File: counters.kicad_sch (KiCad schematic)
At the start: 22 parts, among them J10 Conn_01x10_Socket, J11 Conn_01x06_Socket, J12 Conn_01x10_Socket, J13 Conn_01x03_Socket, J8 Conn_01x10_Socket, J9 Conn_01x06_Socket, SW1 SW_Push, SW2 SW_Push, U3 SSR, U8 bin-to-dec, U9 bin-to-dec

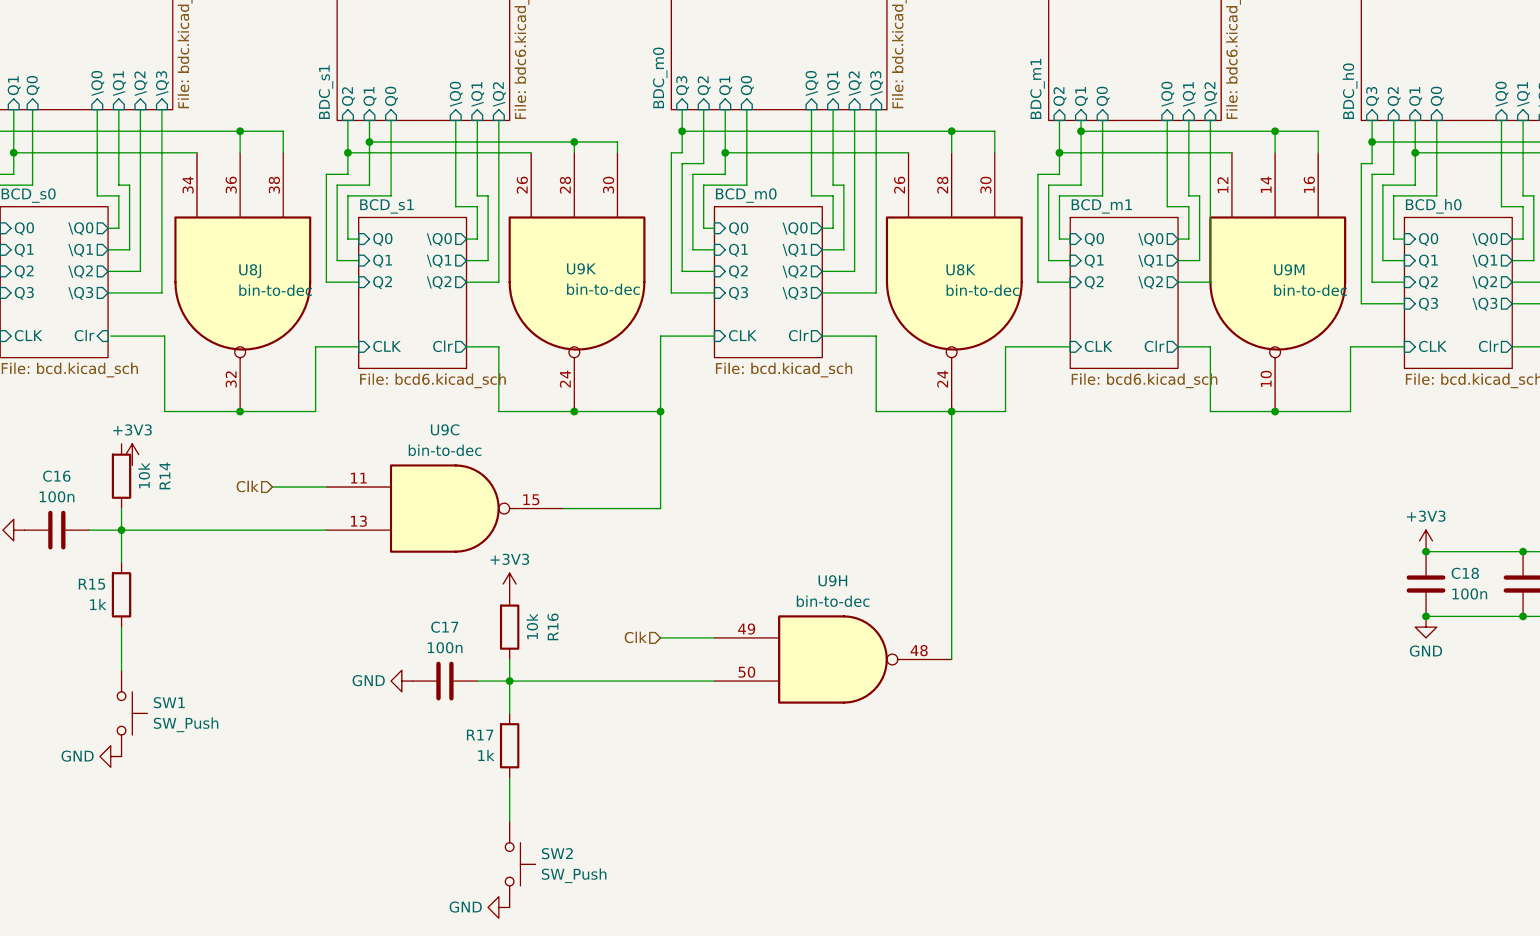
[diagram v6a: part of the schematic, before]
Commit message: some routing on main board
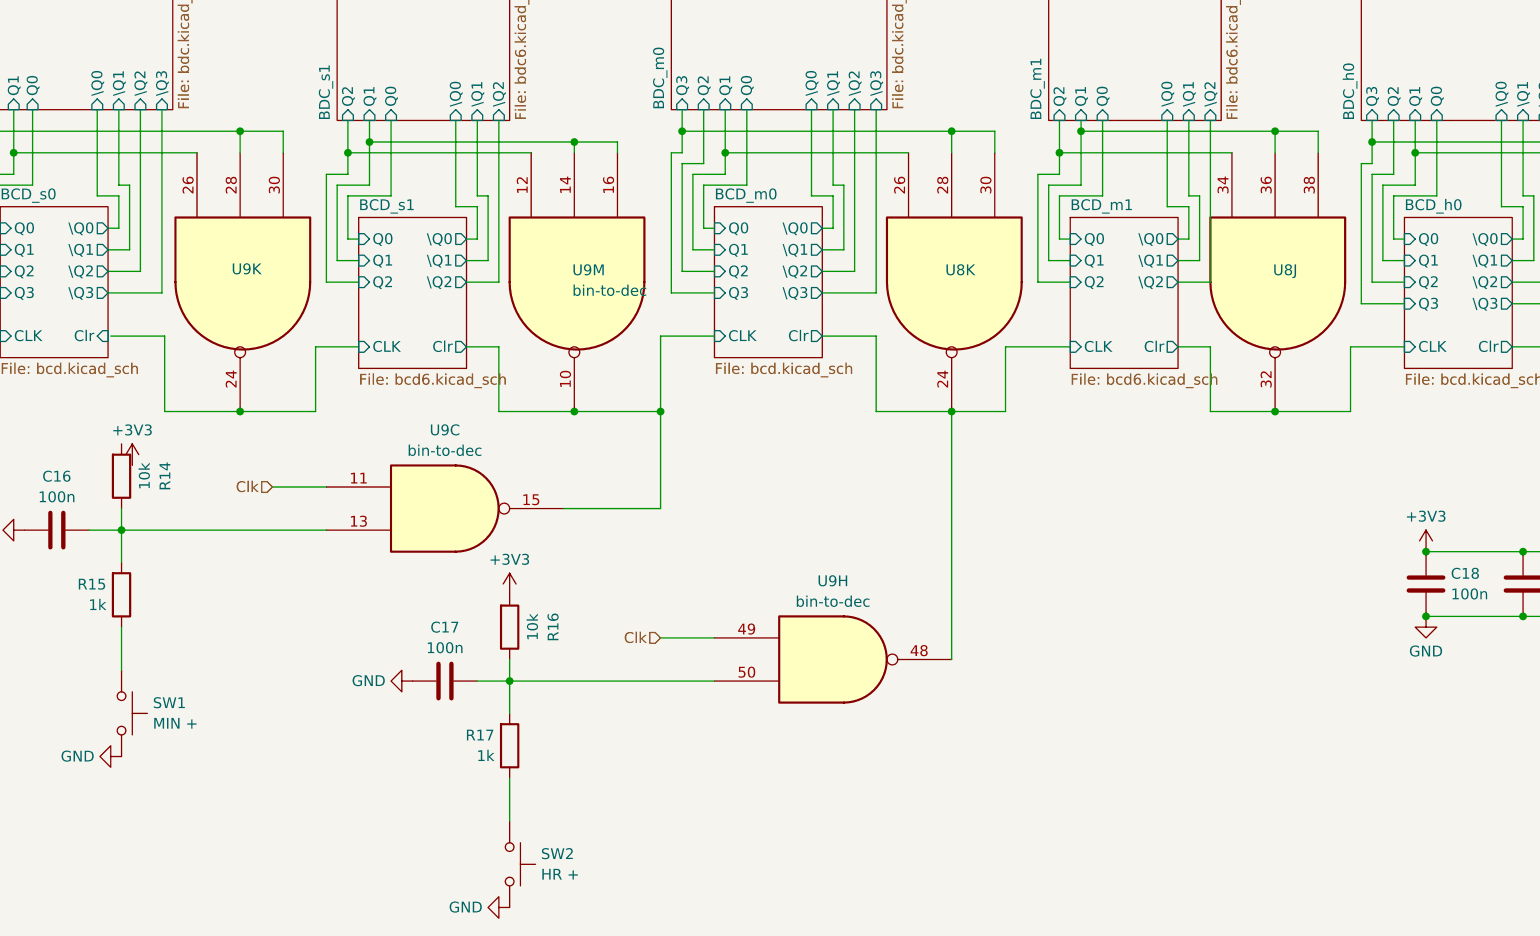
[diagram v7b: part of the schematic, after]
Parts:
- R14, R15, R16, R17: footprint Resistor_SMD:R_0402_1005Metric -> Resistor_SMD:R_0603_1608Metric
- SW1: value SW_Push -> MIN +; footprint Button_Switch_SMD:SW_Push_1P1T_NO_CK_PTS125Sx43PSMTR -> Button_Switch_SMD:SW_SPST_EVQPE1; LCSC Part # (none) -> C720477
- SW2: value SW_Push -> HR +; footprint Button_Switch_SMD:SW_Push_1P1T_NO_CK_PTS125Sx43PSMTR -> Button_Switch_SMD:SW_SPST_EVQPE1; LCSC Part # (none) -> C720477
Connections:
- net BCD_h0/CLK: now also U8.32; no longer U9.10
- net BCD_m0/CLK: now also U9.10; no longer U9.24
- net BCD_m1/Q1: now also U8.36, U8.38; no longer U9.14, U9.16
- net BCD_m1/Q2: now also U8.34; no longer U9.12
- net BCD_s0/Q1: now also U9.26; no longer U8.34
- net BCD_s0/Q3: now also U9.28, U9.30; no longer U8.36, U8.38
- net BCD_s1/CLK: now also U9.24; no longer U8.32
- net BCD_s1/Q1: now also U9.14, U9.16; no longer U9.28, U9.30
- net BCD_s1/Q2: now also U9.12; no longer U9.26
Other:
- moved on the sheet: U8J, U9K, U9M
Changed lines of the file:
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@@
 	(paper "A4")
 	(junction
+		(at 52.07 130.81)
+		(diameter 0)
+		(color 0 0 0 0)
+	)
+	(junction
 		(at 91.44 99.06)
 		(diameter 0)
@@
 	)
 	(junction
-		(at 104.14 97.79)
-		(diameter 0)
-		(color 0 0 0 0)
-	)
-	(junction
-		(at 91.44 130.81)
+		(at 173.99 130.81)
 		(diameter 0)
 		(color 0 0 0 0)
 	)
 	(junction
-		(at 173.99 130.81)
+		(at 104.14 97.79)
 		(diameter 0)
 		(color 0 0 0 0)
@@
 	)
 	(junction
+		(at 91.44 130.81)
+		(diameter 0)
+		(color 0 0 0 0)
+	)
+	(junction
 		(at 148.59 100.33)
 		(diameter 0)
@@
 	)
 	(junction
-		(at 52.07 130.81)
-		(diameter 0)
-		(color 0 0 0 0)
-	)
-	(junction
 		(at 214.63 154.94)
 		(diameter 0)
@@
 	(wire
 		(pts
-			(xy 182.88 130.81) (xy 173.99 130.81)
-		)
-		(stroke
-			(width 0)
-			(type default)
-		)
-	)
-	(wire
-		(pts
 			(xy 109.22 100.33) (xy 109.22 102.87)
 		)
@@
 	(wire
 		(pts
-			(xy 91.44 130.81) (xy 101.6 130.81)
+			(xy 190.5 96.52) (xy 190.5 100.33)
 		)
 		(stroke
@@
 	(wire
 		(pts
-			(xy 190.5 96.52) (xy 190.5 100.33)
+			(xy 161.29 106.68) (xy 161.29 96.52)
 		)
 		(stroke
@@
 	(wire
 		(pts
-			(xy 161.29 106.68) (xy 161.29 96.52)
+			(xy 124.46 77.47) (xy 124.46 71.12)
 		)
 		(stroke
@@
 	(wire
 		(pts
-			(xy 124.46 77.47) (xy 124.46 71.12)
+			(xy 173.99 130.81) (xy 182.88 130.81)
 		)
 		(stroke
@@
 	(wire
 		(pts
-			(xy 52.07 130.81) (xy 60.96 130.81)
-		)
-		(stroke
-			(width 0)
-			(type default)
-		)
-	)
-	(wire
-		(pts
 			(xy 204.47 113.03) (xy 201.93 113.03)
 		)
@@
 	(wire
 		(pts
+			(xy 91.44 130.81) (xy 101.6 130.81)
+		)
+		(stroke
+			(width 0)
+			(type default)
+		)
+	)
+	(wire
+		(pts
 			(xy 147.32 104.14) (xy 147.32 113.03)
 		)
@@
 	(wire
 		(pts
+			(xy 52.07 130.81) (xy 60.96 130.81)
+		)
+		(stroke
+			(width 0)
+			(type default)
+		)
+	)
+	(wire
+		(pts
 			(xy 32.7025 71.12) (xy 32.7025 77.47)
 		)
@@
 	(wire
 		(pts
-			(xy 173.99 130.81) (xy 166.37 130.81)
+			(xy 166.37 130.81) (xy 173.99 130.81)
 		)
 		(stroke
@@
 			)
 		)
-		(property "Footprint" "Resistor_SMD:R_0402_1005Metric"
+		(property "Footprint" "Resistor_SMD:R_0603_1608Metric"
 			(at 36.322 138.43 90)
 			(effects
@@
 			)
 		)
-		(property "Footprint" "Resistor_SMD:R_0402_1005Metric"
+		(property "Footprint" "Resistor_SMD:R_0603_1608Metric"
 			(at 36.322 152.4 90)
 			(effects
@@
 	(symbol
 		(lib_id "custom:BDC_nands")
-		(at 101.6 96.52 270)
+		(at 62.23 96.52 270)
 		(unit 11)
 		(exclude_from_sim no)
@@
 		(dnp no)
 		(property "Reference" "U9"
-			(at 90.424 114.046 90)
+			(at 51.054 114.046 90)
 			(effects
 				(font
@@
 		)
 		(property "Value" "bin-to-dec"
-			(at 90.424 116.4703 90)
+			(at 51.054 116.4703 90)
 			(effects
 				(font
@@
 				)
 				(justify left)
+				(hide yes)
 			)
 		)
 		(property "Footprint" "custom:module_bdc_mpcie"
-			(at 101.6 96.52 0)
+			(at 62.23 96.52 0)
 			(effects
 				(font
@@
 		)
 		(property "Datasheet" ""
-			(at 101.6 96.52 0)
+			(at 62.23 96.52 0)
 			(effects
 				(font
@@
 		)
 		(property "Description" ""
-			(at 101.6 96.52 0)
+			(at 62.23 96.52 0)
 			(effects
 				(font
@@
 		)
 		(property "LCSC Part #" "C185937"
-			(at 101.6 96.52 90)
+			(at 62.23 96.52 90)
 			(effects
 				(font
@@
 			)
 		)
-		(property "Footprint" "Resistor_SMD:R_0402_1005Metric"
+		(property "Footprint" "Resistor_SMD:R_0603_1608Metric"
 			(at 82.042 170.18 90)
 			(effects
@@
 	(symbol
 		(lib_id "custom:BDC_nands")
-		(at 60.96 97.79 270)
+		(at 182.88 97.79 270)
 		(unit 10)
 		(exclude_from_sim no)
@@
 		(dnp no)
 		(property "Reference" "U8"
-			(at 51.816 114.1617 90)
+			(at 173.736 114.1617 90)
 			(effects
 				(font
@@
 		)
 		(property "Value" "bin-to-dec"
-			(at 51.816 116.586 90)
+			(at 173.736 116.586 90)
 			(effects
 				(font
@@
 				)
 				(justify left)
+				(hide yes)
 			)
 		)
 		(property "Footprint" "custom:module_bdc_mpcie"
-			(at 60.96 97.79 0)
+			(at 182.88 97.79 0)
 			(effects
 				(font
@@
 		)
 		(property "Datasheet" ""
-			(at 60.96 97.79 0)
+			(at 182.88 97.79 0)
 			(effects
 				(font
@@
 		)
 		(property "Description" ""
-			(at 60.96 97.79 0)
+			(at 182.88 97.79 0)
 			(effects
 				(font
@@
 		)
 		(property "LCSC Part #" "C185937"
-			(at 60.96 97.79 90)
+			(at 182.88 97.79 90)
 			(effects
 				(font
@@
 			)
 		)
-		(property "Value" "SW_Push"
+		(property "Value" "MIN +"
 			(at 41.783 167.5821 90)
 			(effects
@@
 			)
 		)
-		(property "Footprint" "Button_Switch_SMD:SW_Push_1P1T_NO_CK_PTS125Sx43PSMTR"
+		(property "Footprint" "Button_Switch_SMD:SW_SPST_EVQPE1"
 			(at 43.18 166.37 0)
 			(effects
@@
 			)
 		)
-		(property "LCSC Part #" ""
+		(property "LCSC Part #" "C720477"
 			(at 38.1 166.37 0)
 			(effects
@@
 	(symbol
 		(lib_id "custom:BDC_nands")
-		(at 185.42 96.52 270)
+		(at 102.87 96.52 270)
 		(unit 13)
 		(exclude_from_sim no)
@@
 		(dnp no)
 		(property "Reference" "U9"
-			(at 173.736 114.1617 90)
+			(at 91.186 114.1617 90)
 			(effects
 				(font
@@
 		)
 		(property "Value" "bin-to-dec"
-			(at 173.736 116.586 90)
+			(at 91.186 116.586 90)
 			(effects
 				(font
@@
 		)
 		(property "Footprint" "custom:module_bdc_mpcie"
-			(at 185.42 96.52 0)
+			(at 102.87 96.52 0)
 			(effects
 				(font
@@
 		)
 		(property "Datasheet" ""
-			(at 185.42 96.52 0)
+			(at 102.87 96.52 0)
 			(effects
 				(font
@@
 		)
 		(property "Description" ""
-			(at 185.42 96.52 0)
+			(at 102.87 96.52 0)
 			(effects
 				(font
@@
 		)
 		(property "LCSC Part #" "C185937"
-			(at 185.42 96.52 90)
+			(at 102.87 96.52 90)
 			(effects
 				(font
@@
 				)
 				(justify left)
+				(hide yes)
 			)
 		)
@@
 			)
 		)
-		(property "Value" "SW_Push"
+		(property "Value" "HR +"
 			(at 87.503 185.3621 90)
 			(effects
@@
 			)
 		)
-		(property "Footprint" "Button_Switch_SMD:SW_Push_1P1T_NO_CK_PTS125Sx43PSMTR"
+		(property "Footprint" "Button_Switch_SMD:SW_SPST_EVQPE1"
 			(at 88.9 184.15 0)
 			(effects
@@
 			)
 		)
-		(property "LCSC Part #" ""
+		(property "LCSC Part #" "C720477"
 			(at 83.82 184.15 0)
 			(effects
@@
 			)
 		)
-		(property "Footprint" "Resistor_SMD:R_0402_1005Metric"
+		(property "Footprint" "Resistor_SMD:R_0603_1608Metric"
 			(at 82.042 156.21 90)
 			(effects

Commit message: routy mcRouteface
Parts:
- C16, C17, C18, C19, C20, C21, C22: LCSC Part # C57112 -> C14663
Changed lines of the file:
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@@
 			)
 		)
-		(property "LCSC Part #" "C57112"
+		(property "LCSC Part #" "C14663"
 			(at 191.77 151.13 0)
 			(effects
@@
 			)
 		)
-		(property "LCSC Part #" "C57112"
+		(property "LCSC Part #" "C14663"
 			(at 76.2 162.56 0)
 			(effects
@@
 			)
 		)
-		(property "LCSC Part #" "C57112"
+		(property "LCSC Part #" "C14663"
 			(at 237.49 151.13 0)
 			(effects
@@
 			)
 		)
-		(property "LCSC Part #" "C57112"
+		(property "LCSC Part #" "C14663"
 			(at 214.63 151.13 0)
 			(effects
@@
 			)
 		)
-		(property "LCSC Part #" "C57112"
+		(property "LCSC Part #" "C14663"
 			(at 203.2 151.13 0)
 			(effects
@@
 			)
 		)
-		(property "LCSC Part #" "C57112"
+		(property "LCSC Part #" "C14663"
 			(at 226.06 151.13 0)
 			(effects
@@
 			)
 		)
-		(property "LCSC Part #" "C57112"
+		(property "LCSC Part #" "C14663"
 			(at 30.48 144.78 0)
 			(effects
